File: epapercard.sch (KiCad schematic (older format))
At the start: 2 parts

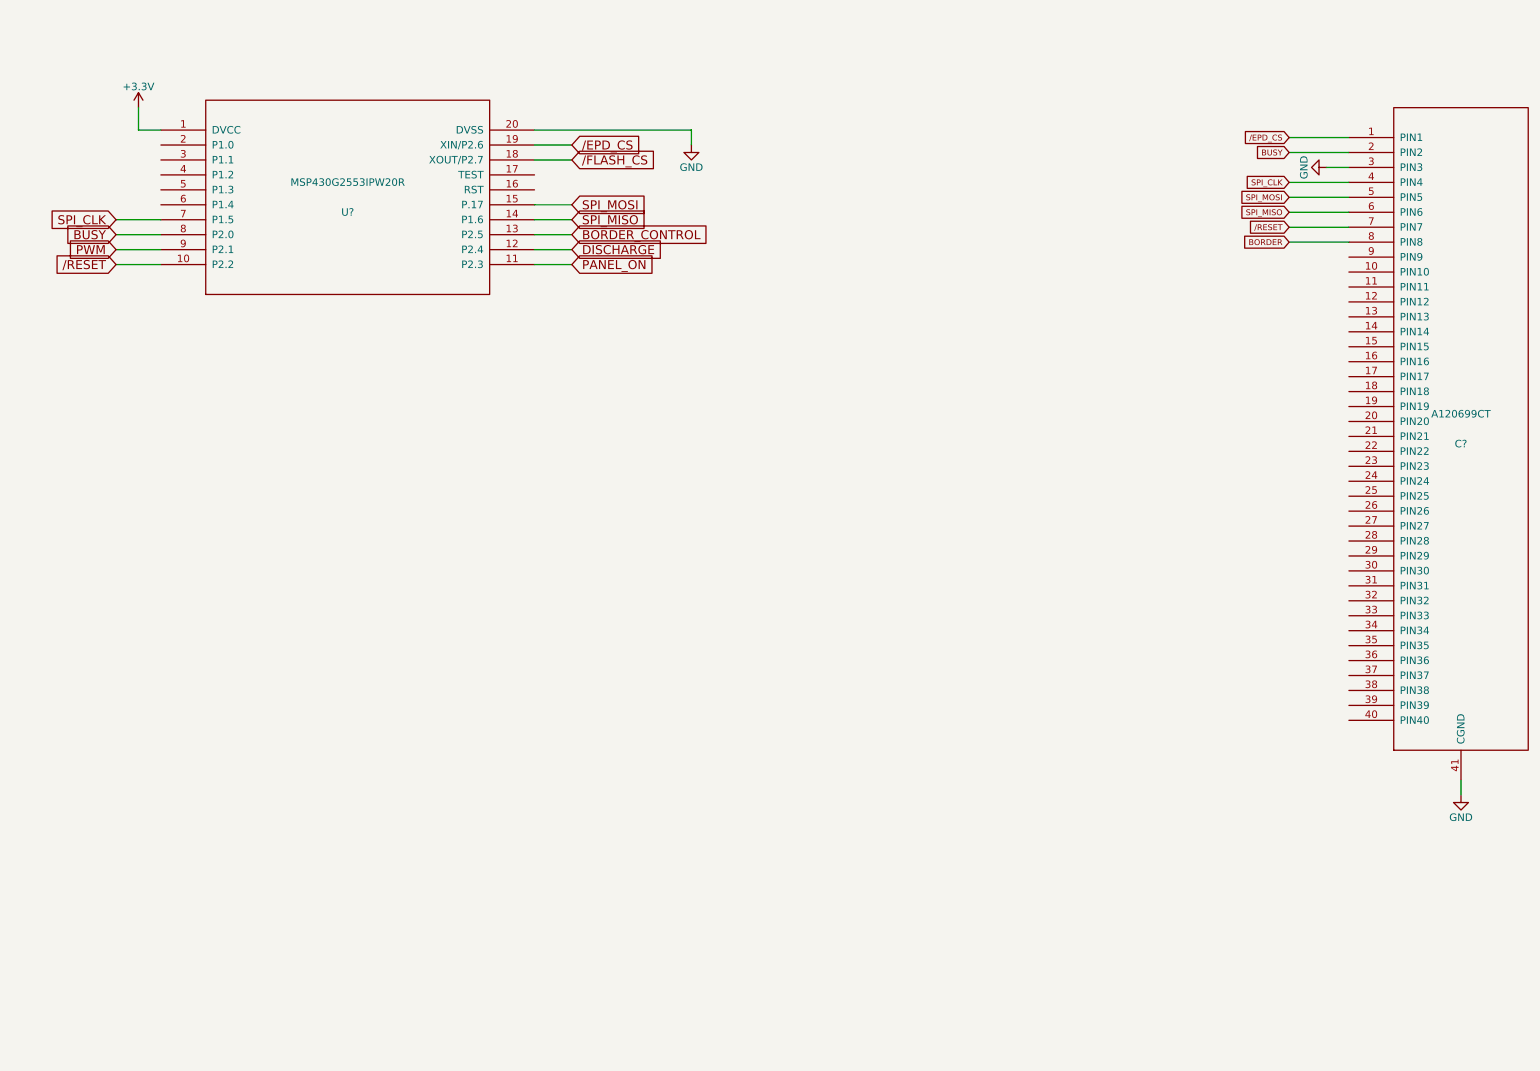
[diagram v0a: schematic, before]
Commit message: Added charge pump caps
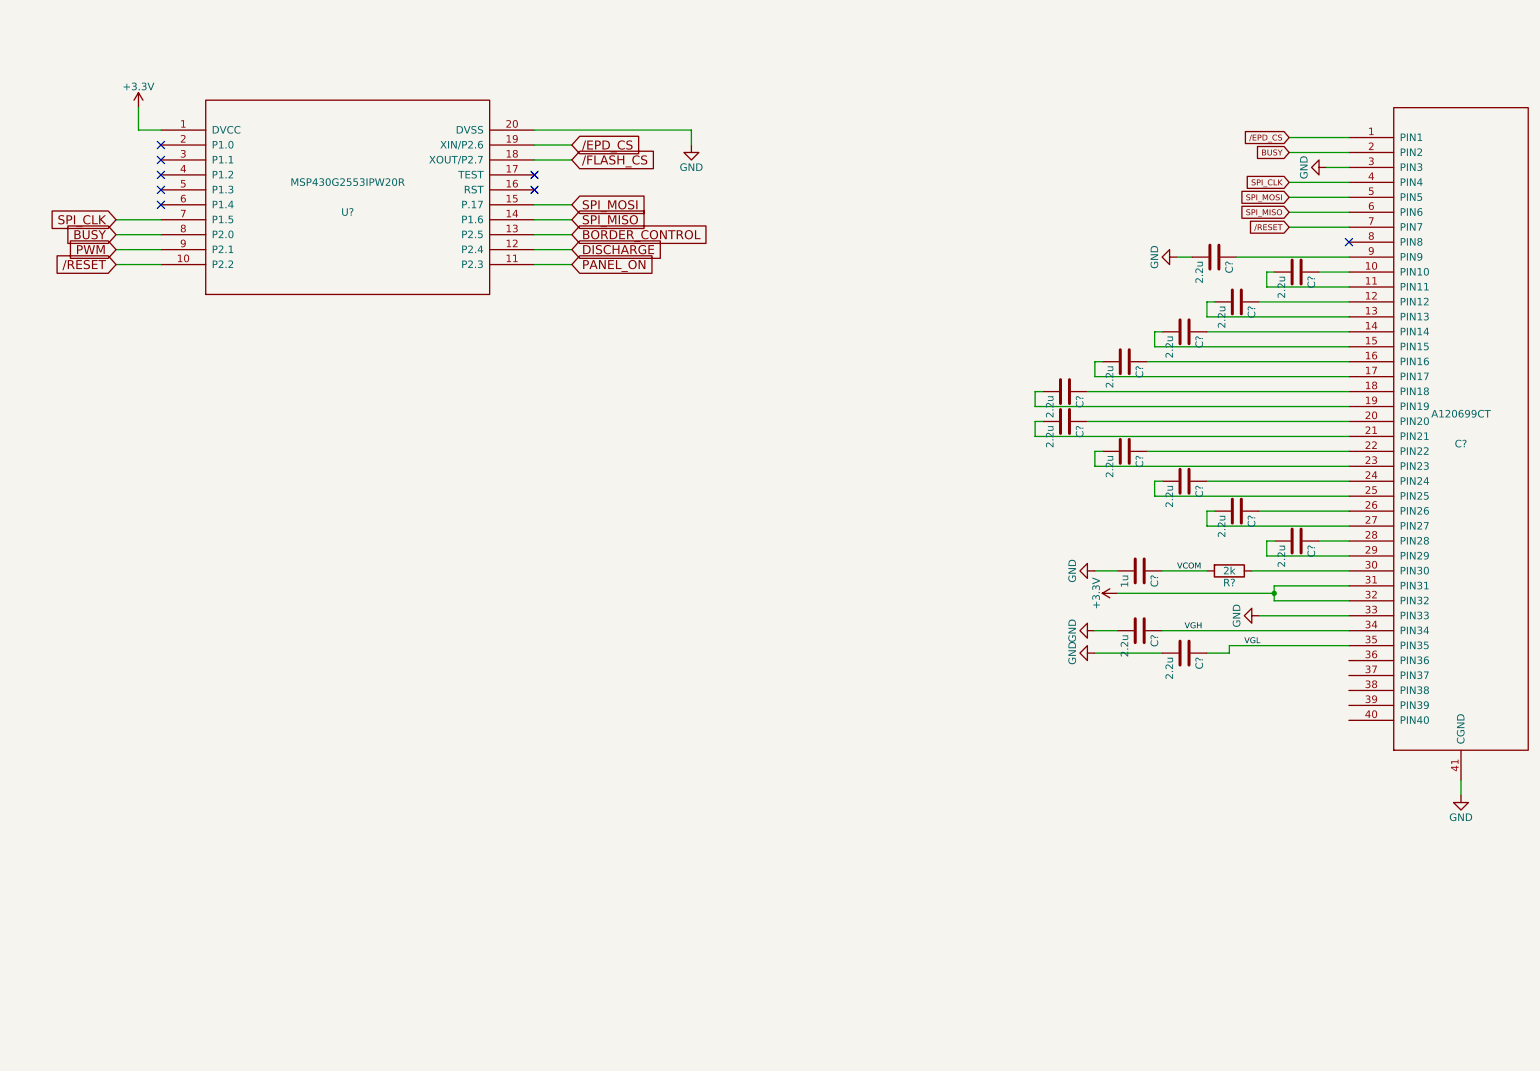
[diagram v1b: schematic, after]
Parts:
- added C? (x13): 2.2u, symbol C
- added C?: 1u, symbol C
- added R?: 2k, symbol R
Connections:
- net +3V3: now also C?.31 (PIN31), C?.32 (PIN32)
- net GND: now also C?.33 (PIN33), C?.2, C?.2, C?.2, C?.2
- net at C?.10 (PIN10): now also C?.1
- net at C?.11 (PIN11): now also C?.2
- net at C?.12 (PIN12): now also C?.1
- net at C?.13 (PIN13): now also C?.2
- net at C?.14 (PIN14): now also C?.1
- net at C?.15 (PIN15): now also C?.2
- net at C?.16 (PIN16): now also C?.1
- net at C?.17 (PIN17): now also C?.2
- net at C?.18 (PIN18): now also C?.1
- net at C?.19 (PIN19): now also C?.2
- net at C?.20 (PIN20): now also C?.1
- net at C?.21 (PIN21): now also C?.2
- net at C?.22 (PIN22): now also C?.1
- net at C?.23 (PIN23): now also C?.2
- net at C?.24 (PIN24): now also C?.1
- net at C?.25 (PIN25): now also C?.2
- net at C?.26 (PIN26): now also C?.1
- net at C?.27 (PIN27): now also C?.2
- net at C?.28 (PIN28): now also C?.1
- net at C?.29 (PIN29): now also C?.2
- net at C?.30 (PIN30): now also R?.1
- net VGH: now reaches C?.34 (PIN34)
- net VGH: now also C?.1
- net VGL: now reaches C?.35 (PIN35)
- net VGL: now also C?.1
- net at C?.9 (PIN9): now also C?.1
- net BORDER: no longer names the net of C?.8 (PIN8)
- new net VCOM: C?.1, R?.2
- no-connect marks 0 -> 8

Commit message: Fixed a few mistakes
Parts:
- added C?: 100n, symbol C
- added C? (x2): 2.2u, symbol C
- added D?: BAT54SW, symbol D_Schottky_x2_Serial_AKC
- added Q? (x3): 2N7002KW, symbol Q_NMOS_GSD
- added Q?: BSS84W, symbol Q_PMOS_GSD
- added R? (x3): 100k, symbol R
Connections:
- net DISCHARGE: now also Q?.1 (G), Q?.1 (G)
- net GND: now also C?.2, C?.2, D?.2 (K), Q?.2 (S)
- net PWM: now also C?.2
- net VCOM: now also C?.39 (PIN39), C?.40 (PIN40), R?.1
- net VGH: now also Q?.3 (D)
- net VGL: now also D?.1 (A)
- net VDH: now reaches C?.36 (PIN36)
- net VDH: now also C?.1, Q?.3 (D)
- net VDL: now reaches C?.37 (PIN37)
- net VDL: now also C?.1, Q?.2 (S), R?.2
- net BORDER: now reaches C?.38 (PIN38)
- net BORDER: now also Q?.3 (D), R?.2
- new net: C?.1, D?.3 (common)
- new net: Q?.1 (G), R?.1, R?.2
- new net: Q?.3 (D), R?.1
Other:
- note added: "Epaper Business Card"

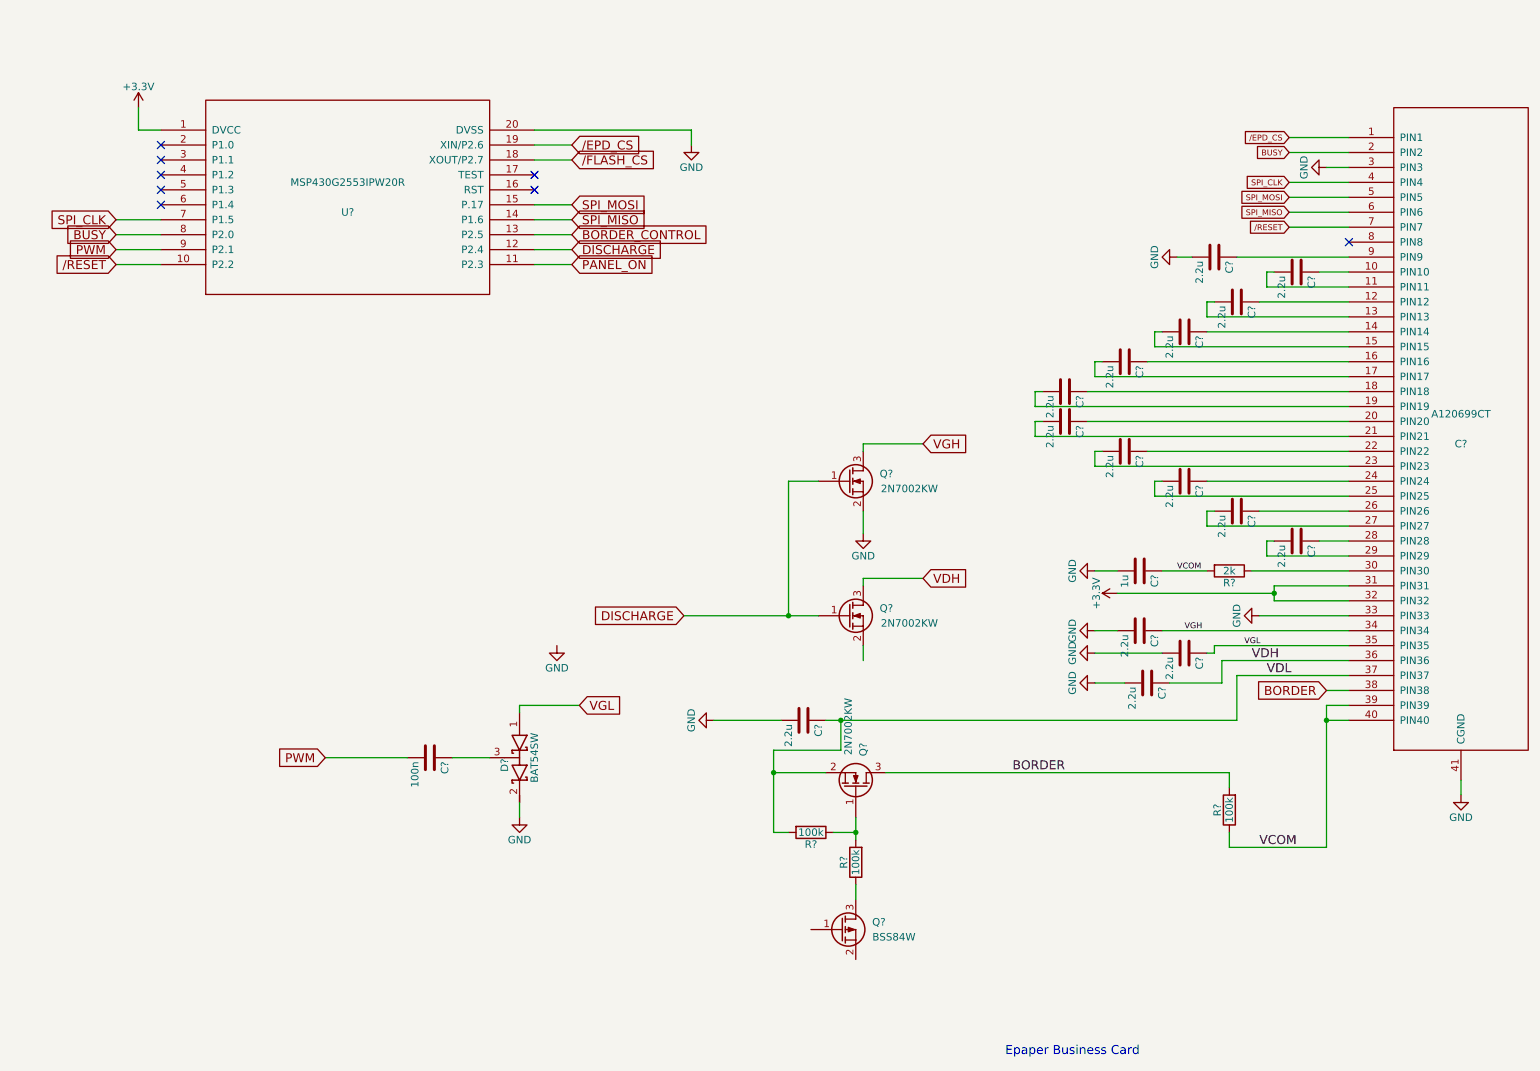
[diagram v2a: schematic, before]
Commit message: Added power circuit
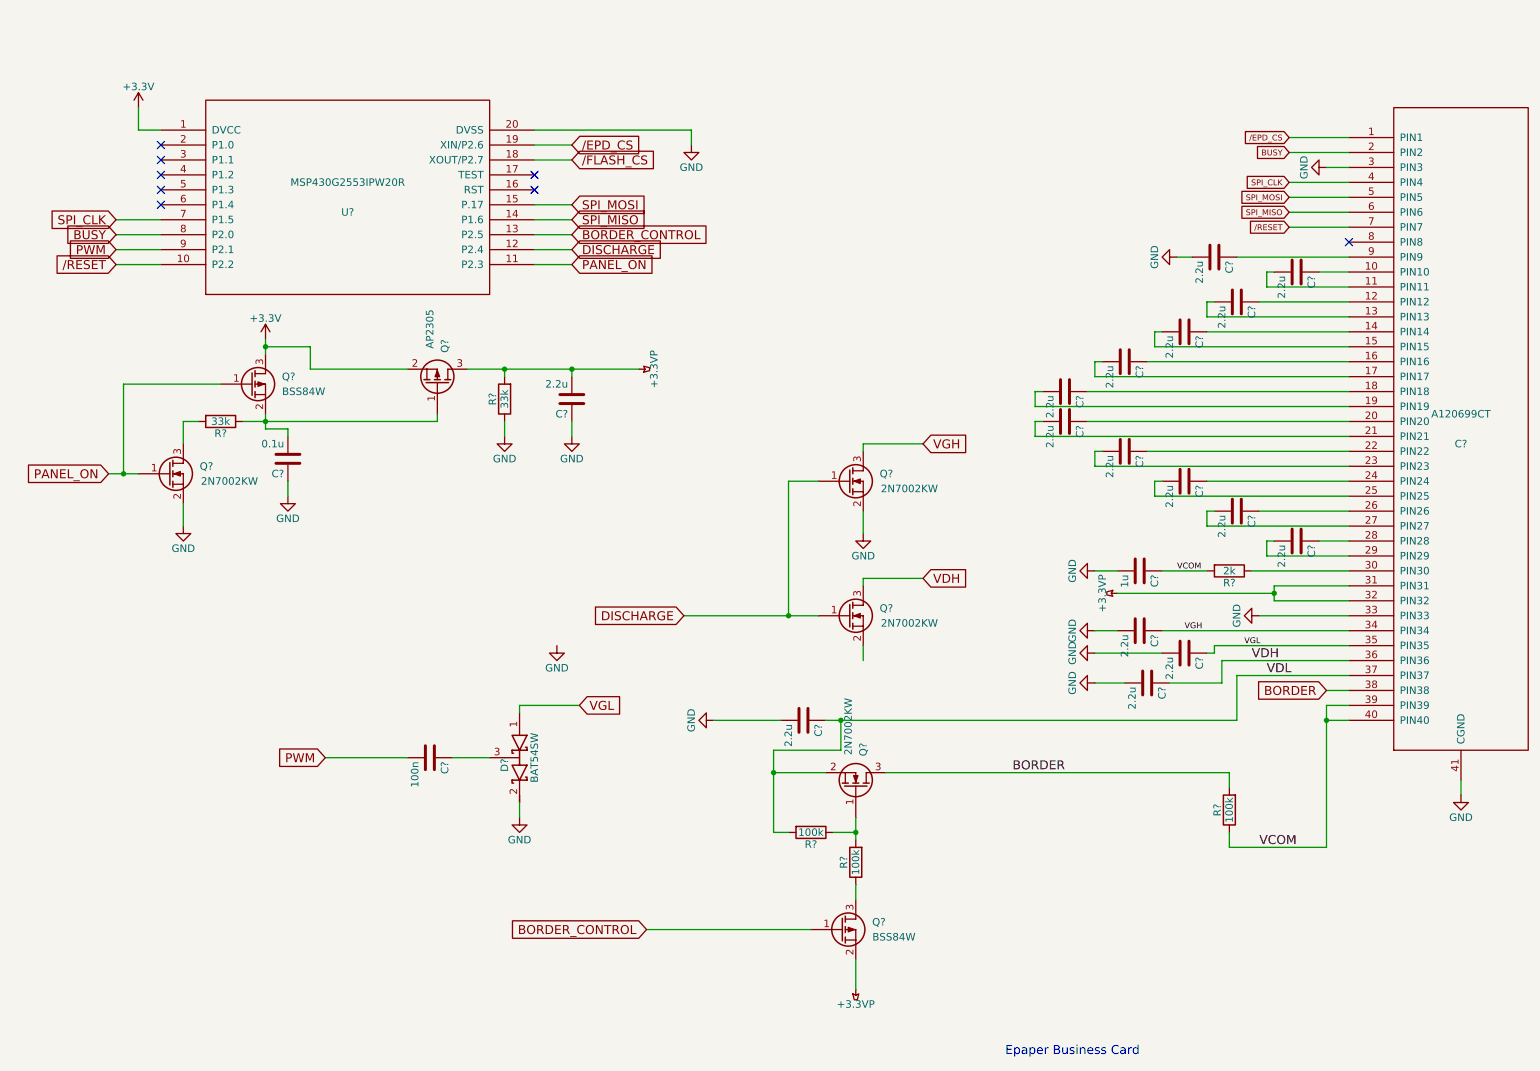
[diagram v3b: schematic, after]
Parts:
- added C?: 0.1u, symbol C
- added C?: 2.2u, symbol C
- added Q?: 2N7002KW, symbol Q_NMOS_GSD
- added Q?: BSS84W, symbol Q_PMOS_GSD
- added Q?: AP2305, symbol Q_PMOS_GSD
- added R? (x2): 33k, symbol R
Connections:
- net +3V3: now also Q?.2 (S), Q?.3 (D); no longer C?.31 (PIN31), C?.32 (PIN32)
- net BORDER_CONTROL: now also Q?.1 (G)
- net GND: now also C?.1, C?.1, Q?.2 (S), R?.1
- net PANEL_ON: now also Q?.1 (G), Q?.1 (G)
- net +3.3VP: now reaches Q?.2 (S)
- net +3.3VP: now also C?.31 (PIN31), C?.32 (PIN32), C?.2, Q?.3 (D), R?.2
- new net: Q?.3 (D), R?.2
- new net: C?.2, Q?.1 (G), Q?.2 (S), R?.1
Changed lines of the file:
@@
 Text Label 8500 4250 0    39   ~ 0
 VCOM
-$Comp
-L +3.3V #PWR?
-U 1 1 57342667
-P 8100 4400
-F 0 "#PWR?" H 8100 4250 50  0001 C CNN
-F 1 "+3.3V" H 8100 4540 50  0000 C CNN
-F 2 "" H 8100 4400 50  0000 C CNN
-F 3 "" H 8100 4400 50  0000 C CNN
-	1    8100 4400
-	0    -1   -1   0
-$EndComp
 Wire Wire Line
 	8100 4400 9150 4400
@@
 Wire Wire Line
 	6350 6350 6350 6450
+$Comp
+L +3.3VP #PWR?
+U 1 1 5734E1DE
+P 8100 4400
+F 0 "#PWR?" H 8250 4350 50  0001 C CNN
+F 1 "+3.3VP" H 8100 4500 50  0000 C CNN
+F 2 "" H 8100 4400 50  0000 C CNN
+F 3 "" H 8100 4400 50  0000 C CNN
+	1    8100 4400
+	0    -1   -1   0
+$EndComp
+$Comp
+L +3.3VP #PWR?
+U 1 1 5734E474
+P 6350 7050
+F 0 "#PWR?" H 6500 7000 50  0001 C CNN
+F 1 "+3.3VP" H 6350 7150 50  0000 C CNN
+F 2 "" H 6350 7050 50  0000 C CNN
+F 3 "" H 6350 7050 50  0000 C CNN
+	1    6350 7050
+	-1   0    0    1
+$EndComp
+Wire Wire Line
+	6350 7050 6350 6850
+Wire Wire Line
+	6050 6650 4950 6650
+Text GLabel 4950 6650 0    60   Input ~ 0
+BORDER_CONTROL
+$Comp
+L +3.3V #PWR?
+U 1 1 5734EA4E
+P 2400 2700
+F 0 "#PWR?" H 2400 2550 50  0001 C CNN
+F 1 "+3.3V" H 2400 2840 50  0000 C CNN
+F 2 "" H 2400 2700 50  0000 C CNN
+F 3 "" H 2400 2700 50  0000 C CNN
+	1    2400 2700
+	1    0    0    -1
+$EndComp
+$Comp
+L Q_NMOS_GSD Q?
+U 1 1 5734EB01
+P 1750 3600
+F 0 "Q?" H 2050 3650 50  0000 R CNN
+F 1 "2N7002KW" H 2350 3550 50  0000 R CNN
+F 2 "" H 1950 3700 50  0000 C CNN
+F 3 "" H 1750 3600 50  0000 C CNN
+	1    1750 3600
+	1    0    0    -1
+$EndComp
+$Comp
+L Q_PMOS_GSD Q?
+U 1 1 5734EF20
+P 2300 3000
+F 0 "Q?" H 2600 3050 50  0000 R CNN
+F 1 "BSS84W" H 2800 2950 50  0000 R CNN
+F 2 "" H 2500 3100 50  0000 C CNN
+F 3 "" H 2300 3000 50  0000 C CNN
+	1    2300 3000
+	1    0    0    -1
+$EndComp
+$Comp
+L Q_PMOS_GSD Q?
+U 1 1 5734F180
+P 3550 3000
+F 0 "Q?" H 3850 3050 50  0000 R CNN
+F 1 "AP2305" H 4050 2950 50  0000 R CNN
+F 2 "" H 3750 3100 50  0000 C CNN
+F 3 "" H 3550 3000 50  0000 C CNN
+	1    3550 3000
+	0    1    -1   0
+$EndComp
+Wire Wire Line
+	1350 3600 1550 3600
+Text GLabel 1350 3600 0    60   Input ~ 0
+PANEL_ON
+Wire Wire Line
+	1450 3600 1450 3000
+Wire Wire Line
+	1450 3000 2100 3000
+Connection ~ 1450 3600
+$Comp
+L GND #PWR?
+U 1 1 5734F778
+P 1850 3950
+F 0 "#PWR?" H 1850 3700 50  0001 C CNN
+F 1 "GND" H 1850 3800 50  0000 C CNN
+F 2 "" H 1850 3950 50  0000 C CNN
+F 3 "" H 1850 3950 50  0000 C CNN
+	1    1850 3950
+	1    0    0    -1
+$EndComp
+Wire Wire Line
+	1850 3950 1850 3800
+$Comp
+L C C?
+U 1 1 5734FA17
+P 2550 3500
+F 0 "C?" H 2575 3600 50  0000 L CNN
+F 1 "0.1u" H 2575 3400 50  0000 L CNN
+F 2 "" H 2588 3350 50  0000 C CNN
+F 3 "" H 2550 3500 50  0000 C CNN
+	1    2550 3500
+	-1   0    0    1
+$EndComp
+Wire Wire Line
+	2550 3350 2550 3300
+Wire Wire Line
+	2550 3300 2400 3300
+Wire Wire Line
+	2400 3300 2400 3200
+$Comp
+L R R?
+U 1 1 5734FD79
+P 2100 3250
+F 0 "R?" V 2180 3250 50  0000 C CNN
+F 1 "33k" V 2100 3250 50  0000 C CNN
+F 2 "" V 2030 3250 50  0000 C CNN
+F 3 "" H 2100 3250 50  0000 C CNN
+	1    2100 3250
+	0    1    1    0
+$EndComp
+Wire Wire Line
+	1850 3400 1850 3250
+Wire Wire Line
+	1850 3250 1950 3250
+Wire Wire Line
+	2250 3250 3550 3250
+Connection ~ 2400 3250
+$Comp
+L GND #PWR?
+U 1 1 5735025D
+P 2550 3750
+F 0 "#PWR?" H 2550 3500 50  0001 C CNN
+F 1 "GND" H 2550 3600 50  0000 C CNN
+F 2 "" H 2550 3750 50  0000 C CNN
+F 3 "" H 2550 3750 50  0000 C CNN
+	1    2550 3750
+	1    0    0    -1
+$EndComp
+Wire Wire Line
+	2550 3750 2550 3650
+Wire Wire Line
+	2400 2800 2400 2700
+Wire Wire Line
+	3350 2900 2700 2900
+Wire Wire Line
+	2700 2900 2700 2750
+Wire Wire Line
+	2700 2750 2400 2750
+Connection ~ 2400 2750
+Wire Wire Line
+	3550 3250 3550 3200
+$Comp
+L R R?
+U 1 1 57350900
+P 4000 3100
+F 0 "R?" V 4080 3100 50  0000 C CNN
+F 1 "33k" V 4000 3100 50  0000 C CNN
+F 2 "" V 3930 3100 50  0000 C CNN
+F 3 "" H 4000 3100 50  0000 C CNN
+	1    4000 3100
+	-1   0    0    1
+$EndComp
+$Comp
+L C C?
+U 1 1 57350A04
+P 4450 3100
+F 0 "C?" H 4475 3200 50  0000 L CNN
+F 1 "2.2u" H 4475 3000 50  0000 L CNN
+F 2 "" H 4488 2950 50  0000 C CNN
+F 3 "" H 4450 3100 50  0000 C CNN
+	1    4450 3100
+	-1   0    0    1
+$EndComp
+Wire Wire Line
+	3750 2900 4900 2900
+Wire Wire Line
+	4000 2900 4000 2950
+Wire Wire Line
+	4450 2900 4450 2950
+Connection ~ 4000 2900
+Connection ~ 4450 2900
+$Comp
+L GND #PWR?
+U 1 1 57350E2E
+P 4000 3350
+F 0 "#PWR?" H 4000 3100 50  0001 C CNN
+F 1 "GND" H 4000 3200 50  0000 C CNN
+F 2 "" H 4000 3350 50  0000 C CNN
+F 3 "" H 4000 3350 50  0000 C CNN
+	1    4000 3350
+	1    0    0    -1
+$EndComp
+$Comp
+L GND #PWR?
+U 1 1 57350EA2
+P 4450 3350
+F 0 "#PWR?" H 4450 3100 50  0001 C CNN
+F 1 "GND" H 4450 3200 50  0000 C CNN
+F 2 "" H 4450 3350 50  0000 C CNN
+F 3 "" H 4450 3350 50  0000 C CNN
+	1    4450 3350
+	1    0    0    -1
+$EndComp
+Wire Wire Line
+	4000 3350 4000 3250
+Wire Wire Line
+	4450 3350 4450 3250
+$Comp
+L +3.3VP #PWR?
+U 1 1 57351212
+P 4900 2900
+F 0 "#PWR?" H 5050 2850 50  0001 C CNN
+F 1 "+3.3VP" H 4900 3000 50  0000 C CNN
+F 2 "" H 4900 2900 50  0000 C CNN
+F 3 "" H 4900 2900 50  0000 C CNN
+	1    4900 2900
+	0    1    1    0
+$EndComp
 $EndSCHEMATC
